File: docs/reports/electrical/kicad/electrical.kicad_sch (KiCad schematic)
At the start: 34 parts, among them U1 pack, U10 ark-fpv, U11 radiomaster-rp2-v2, U12 benewake-tf-luna, U13 module-socket, U14 pjrc-teensy-41, U15 adafruit-lsm6dsox, U16 cjmcu-5018, U17 pololu-d36v6f3, U18 safety-monitor-buffers, U19 bat54c-on-adapter, U2 base-wiring, U20 module-plug, U21 ark-gps, U22 rpi-5-4gb, U23 rpi-active-cooler, U24 rpi-camera-module-3, U25 heltec-ht-hc01p, U26 module-plug, U27 ark-cannode, U28 fruity-chutes-harrier-40-42, U29 p-chute-switch, U3 holybro-tekko32-f4-50a, U30 pololu-d36v6f3, U31 p-servo-diodes, U32 module-plug, U33 ark-cannode, U34 claws-placeholder, U4 emax-e3-2814-850kv, U5 emax-e3-2814-850kv, U6 emax-e3-2814-850kv, U7 emax-e3-2814-850kv, U8 branch-fuses, U9 matek-bec12s-pro

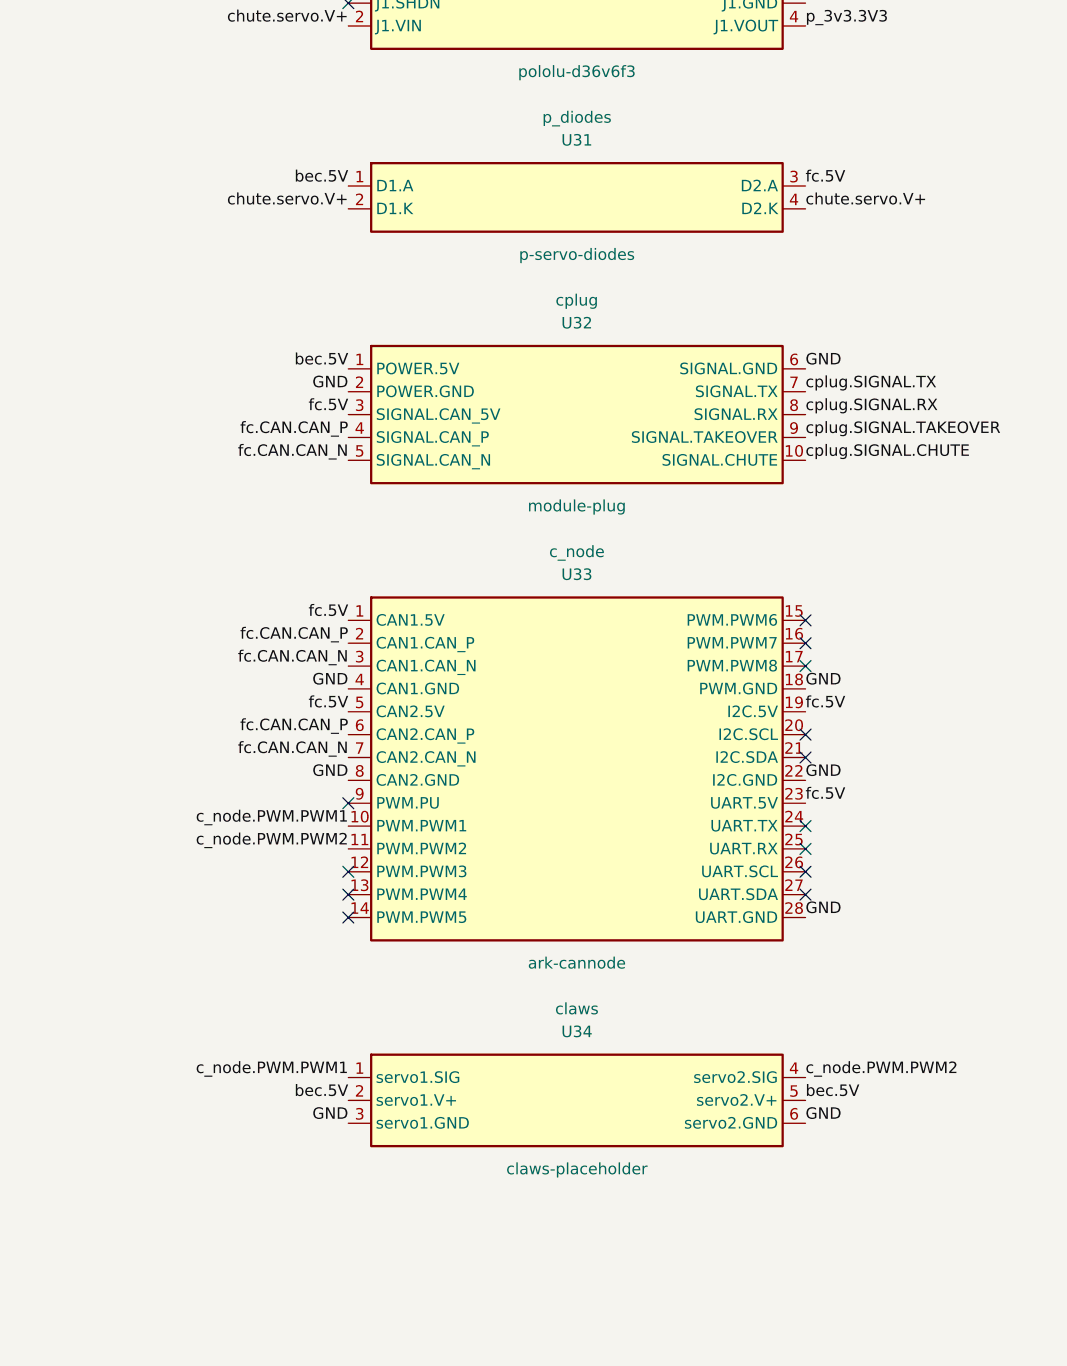
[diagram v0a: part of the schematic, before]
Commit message: The release servo's feed is an ideal-diode OR: TI's LM66200 on Adafruit's board
The two 1N5817 Schottkys dropped the servo to 4.79 V, and 4.54 V on its backup, against 4.9.
On TI's worst-case 60 mOhm it gets 5.16 to 5.20 V, and 4.92 V on the backup, so both findings
are gone. The servo is still a stand-in until Fruity Chutes gives its real range.

Co-Authored-By: Claude Opus 5.5 <noreply@anthropic.com>
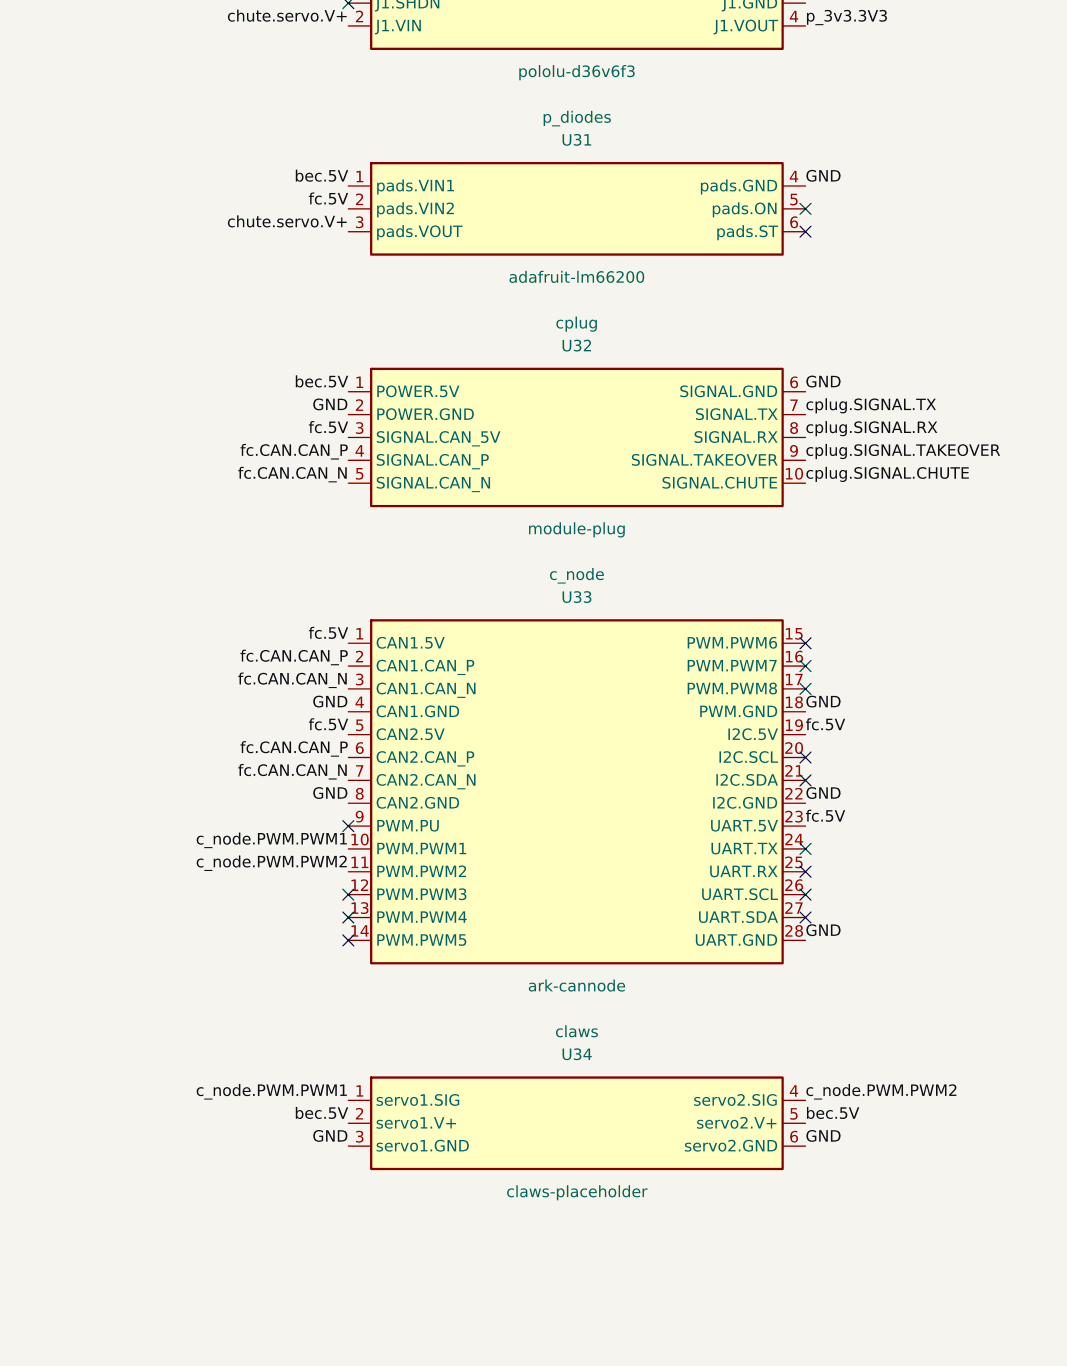
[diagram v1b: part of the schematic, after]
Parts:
- U31: value p-servo-diodes -> adafruit-lm66200; symbol pcs14:p-servo-diodes -> pcs14:adafruit-lm66200
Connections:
- net GND: now also U31.4 (pads.GND)
- net chute.servo.V+: now also U31.3 (pads.VOUT); no longer U31.2 (D1.K), U31.4 (D2.K)
- net fc.5V: now also U31.2 (pads.VIN2); no longer U31.3 (D2.A)
- no-connect marks 85 -> 87
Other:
- moved on the sheet: U32, U33, U34
